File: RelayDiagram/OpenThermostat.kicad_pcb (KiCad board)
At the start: 2 copper layers, 81 parts, among them J1 Conn_01x08_Female, J2 Conn_01x15_Female, J3 Conn_01x15_Female, J4 Conn_01x09_Female, Q1 Q_NMOS_DGS, Q10 Q_NMOS_DGS, Q11 Q_NMOS_DGS, Q12 Q_NMOS_DGS, Q2 Q_NMOS_DGS, Q3 Q_NMOS_DGS, Q4 Q_NMOS_DGS, Q5 Q_NMOS_DGS, Q6 Q_NMOS_DGS, Q7 Q_NMOS_DGS, Q8 Q_NMOS_DGS, Q9 Q_NMOS_DGS, U1 PCF8574, U3 DHT11, U4 EE2-3TNU-L_DPDT_Relay, U5 EE2-3TNU-L_DPDT_Relay, U6 EE2-3TNU-L_DPDT_Relay, U7 EE2-3TNU-L_DPDT_Relay, U8 EE2-3TNU-L_DPDT_Relay, U9 EE2-3TNU-L_DPDT_Relay

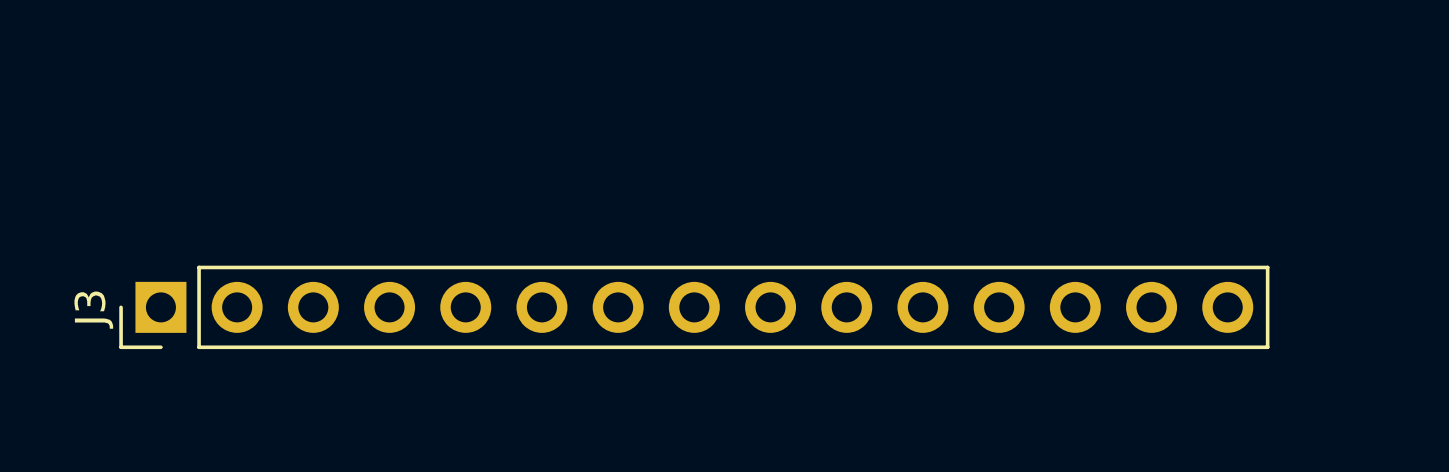
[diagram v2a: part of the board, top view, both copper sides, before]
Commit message: Minor routing changes and placeholder LCD footprint added
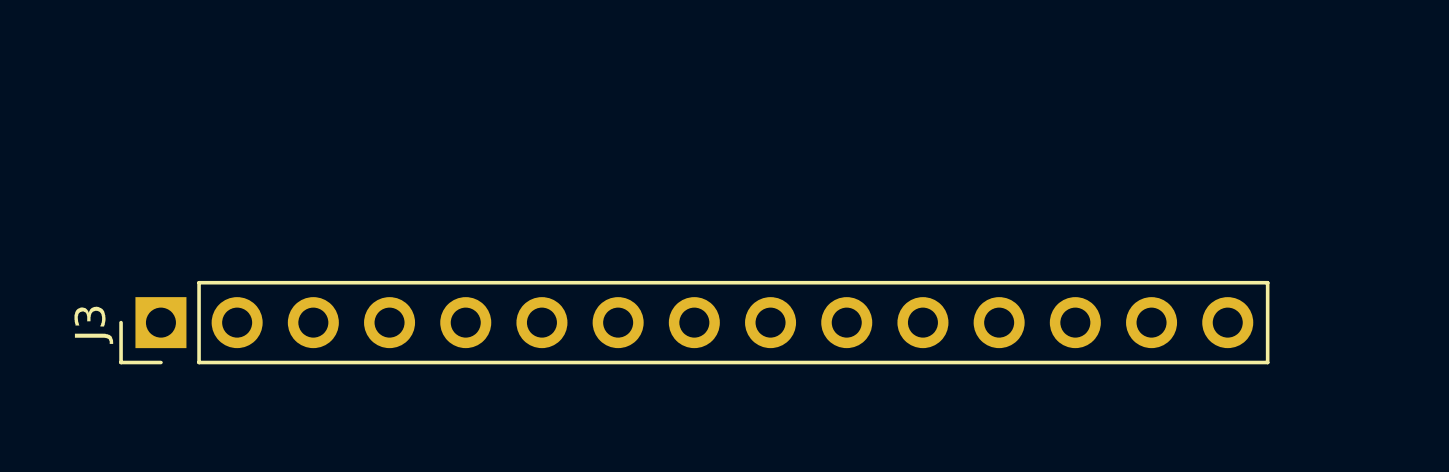
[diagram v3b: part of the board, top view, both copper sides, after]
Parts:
- moved J3 0.51 mm to (53.8, 126.2)
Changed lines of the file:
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@@
   )
   (setup
-    (last_trace_width 0.254)
+    (last_trace_width 0.25)
     (user_trace_width 0.254)
     (user_trace_width 0.508)
@@
   )
   (module Pin_Headers:Pin_Header_Straight_1x15_Pitch2.54mm (layer F.Cu)
-    (at 53.848 125.73 90)
+    (at 53.848 126.238 90)
     (descr "Through hole straight pin header, 1x15, 2.54mm pitch, single row")
     (tags "Through hole pin header THT 1x15 2.54mm single row")
@@
   )
   (dimension 27.94 (width 0.3) (layer F.SilkS)
-    (gr_text "27.940 mm" (at 51.376 113.538 90) (layer F.SilkS)
+    (gr_text "27.940 mm" (at 39.81 113.538 270) (layer F.SilkS)
       (effects (font (size 1.5 1.5) (thickness 0.3)))
     )
-    (feature1 (pts (xy 49.276 99.568) (xy 49.862421 99.568)))
-    (feature2 (pts (xy 49.276 127.508) (xy 49.862421 127.508)))
-    (crossbar (pts (xy 49.276 127.508) (xy 49.276 99.568)))
-    (arrow1a (pts (xy 49.276 99.568) (xy 49.862421 100.694504)))
-    (arrow1b (pts (xy 49.276 99.568) (xy 48.689579 100.694504)))
-    (arrow2a (pts (xy 49.276 127.508) (xy 49.862421 126.381496)))
-    (arrow2b (pts (xy 49.276 127.508) (xy 48.689579 126.381496)))
+    (feature1 (pts (xy 48.006 127.508) (xy 41.323579 127.508)))
+    (feature2 (pts (xy 48.006 99.568) (xy 41.323579 99.568)))
+    (crossbar (pts (xy 41.91 99.568) (xy 41.91 127.508)))
+    (arrow1a (pts (xy 41.91 127.508) (xy 41.323579 126.381496)))
+    (arrow1b (pts (xy 41.91 127.508) (xy 42.496421 126.381496)))
+    (arrow2a (pts (xy 41.91 99.568) (xy 41.323579 100.694504)))
+    (arrow2b (pts (xy 41.91 99.568) (xy 42.496421 100.694504)))
   )
   (via (at 63.1698 91.3892) (size 0.8) (drill 0.4) (layers F.Cu B.Cu) (net 25))

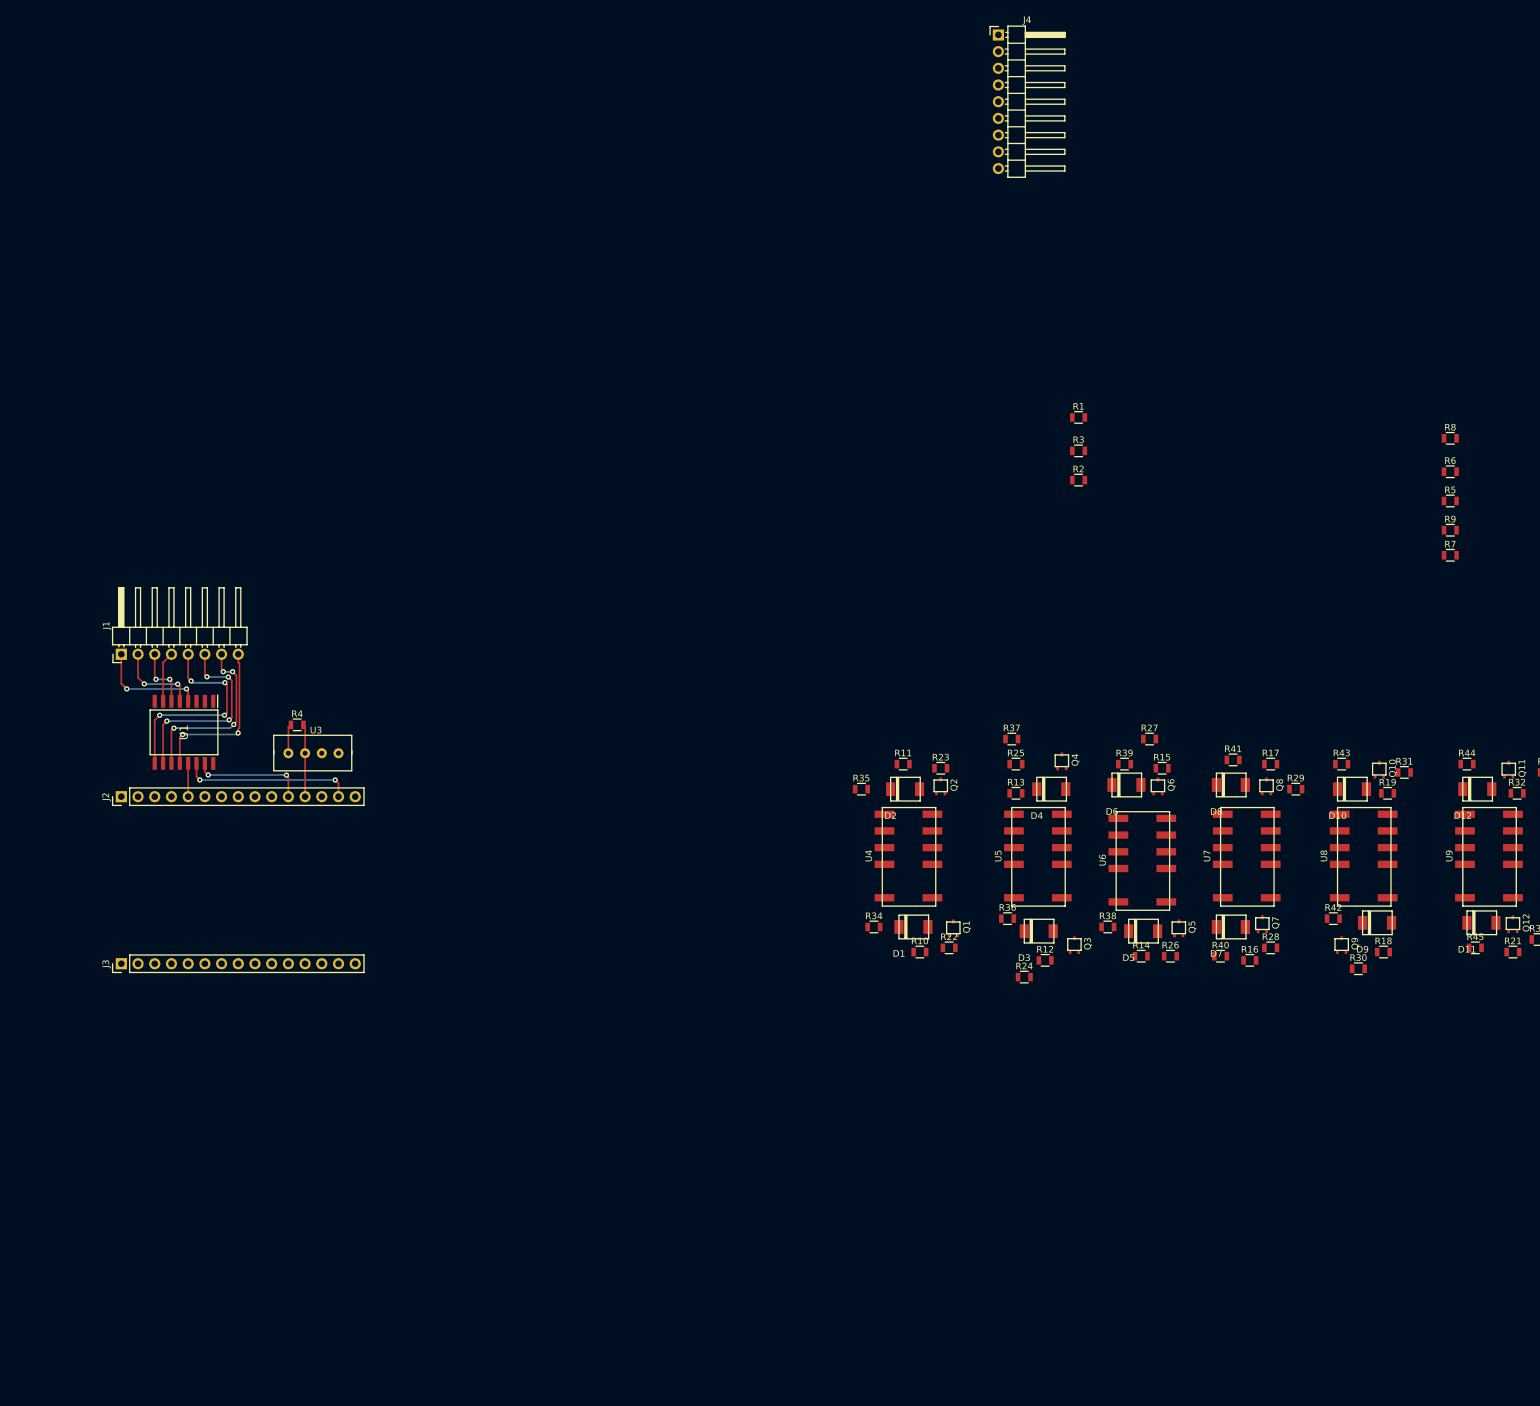
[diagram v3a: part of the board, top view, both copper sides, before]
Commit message: Added button footprints, PCB layout changes, changed schematic to fix relay coil polarity and also changed diode footprints.
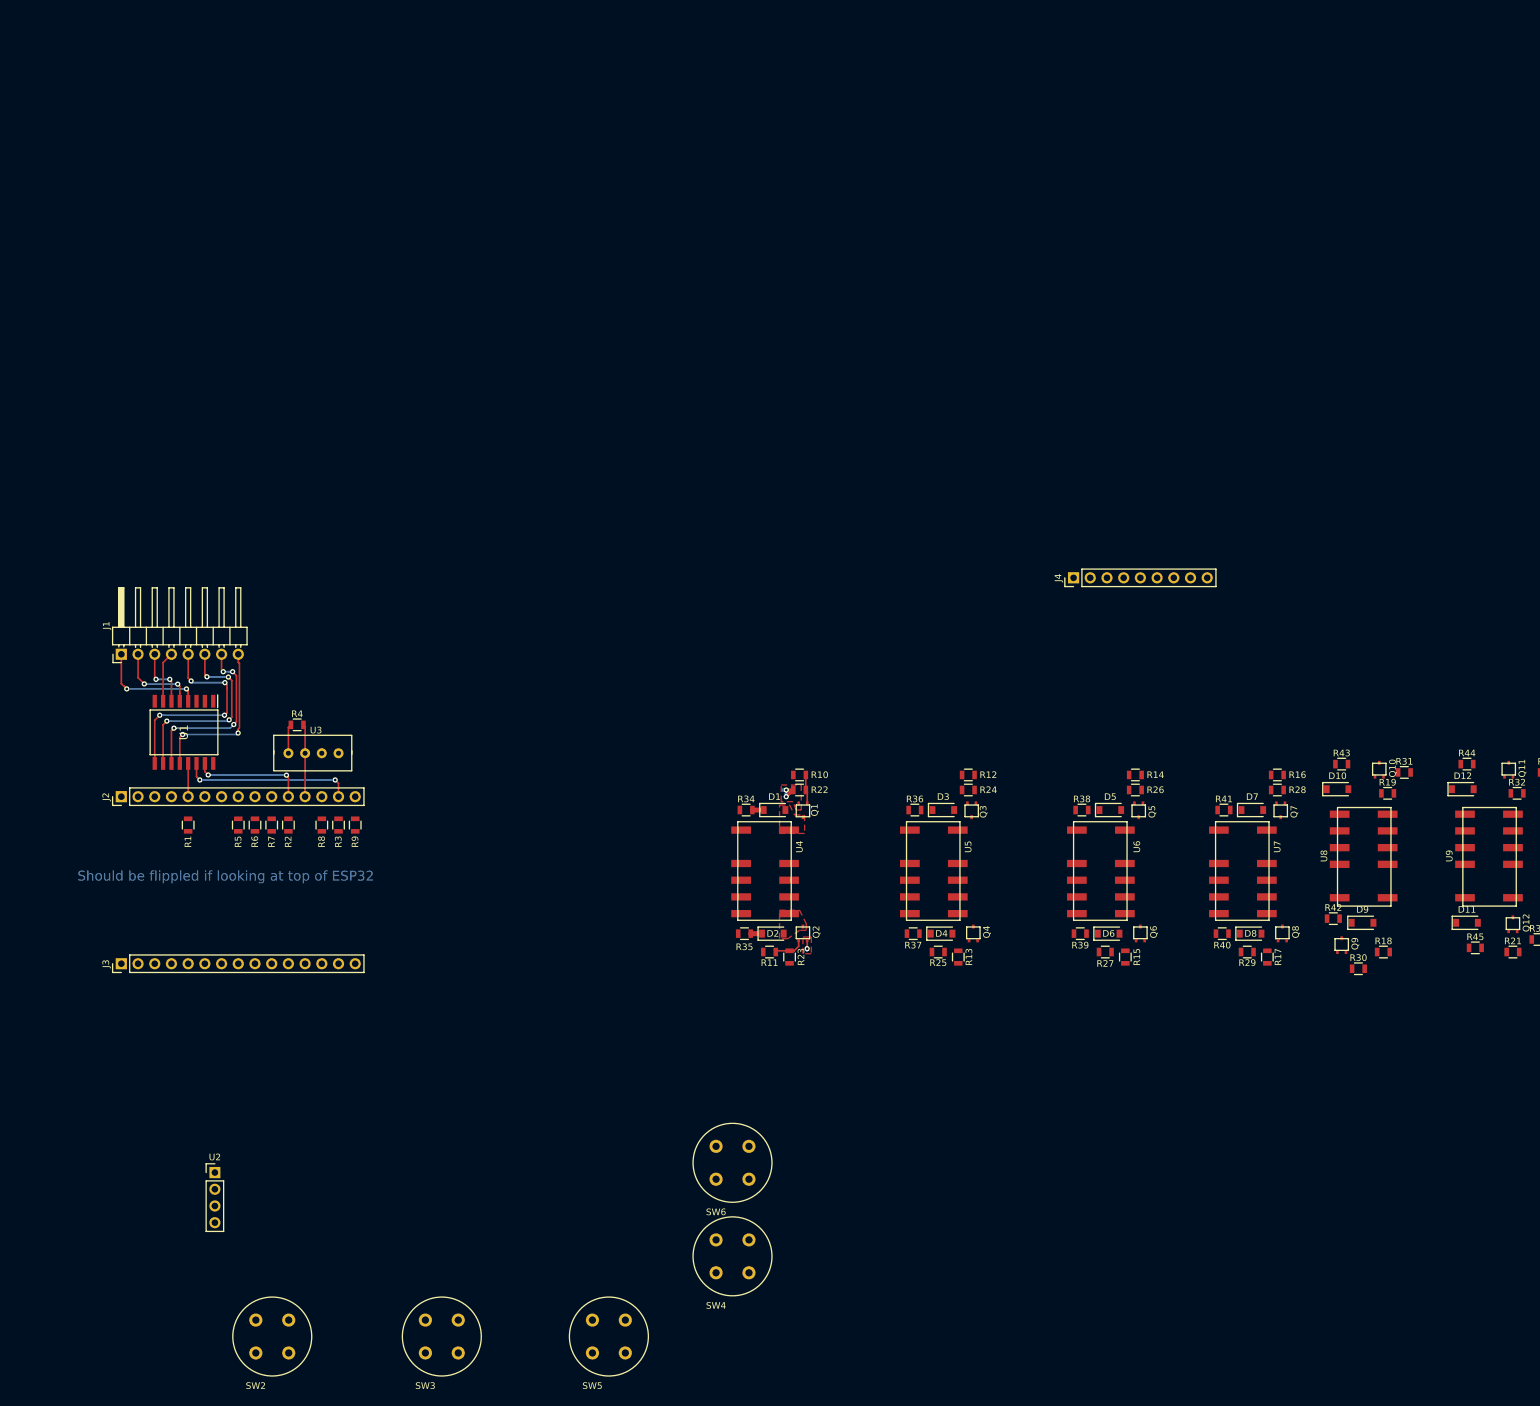
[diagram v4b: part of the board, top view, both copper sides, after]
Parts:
- added SW2: SW_Push, SeniorDesign:Pushbutton-KS-01Q-01, F.Cu at (74.3, 185.4)
- added SW3: SW_Push, SeniorDesign:Pushbutton-KS-01Q-01, F.Cu at (100.1, 185.4)
- added SW4: SW_Push, SeniorDesign:Pushbutton-KS-01Q-01, F.Cu at (144.3, 173.2)
- added SW5: SW_Push, SeniorDesign:Pushbutton-KS-01Q-01, F.Cu at (125.5, 185.4)
- added SW6: SW_Push, SeniorDesign:Pushbutton-KS-01Q-01, F.Cu at (144.3, 159.0)
- added U2: LCD, Pin_Headers:Pin_Header_Straight_1x04_Pitch2.54mm, F.Cu at (68.1, 158.0)
- D1, D10, D11, D12, D2, D3, D4, D5, D6, D7, D8, D9: footprint SeniorDesign:SOD-128-Diode -> Diodes_SMD:D_SOD-123
- J4: footprint Pin_Headers:Pin_Header_Angled_1x09_Pitch2.54mm -> Pin_Headers:Pin_Header_Straight_1x09_Pitch2.54mm
- moved R5 190.8 mm to (71.6, 105.2), turned to 270 degrees
- moved R6 189.5 mm to (74.2, 105.2), turned to 270 degrees
- moved R7 183.8 mm to (76.7, 105.2), turned to 270 degrees
- moved R8 181.4 mm to (84.3, 105.2), turned to 270 degrees
- moved R9 172.4 mm to (89.4, 105.2), turned to 270 degrees
- moved R1 148.9 mm to (64.0, 105.2), turned to 270 degrees
- moved R2 131.1 mm to (79.2, 105.2), turned to 270 degrees
- moved R3 126.1 mm to (86.9, 105.2), turned to 90 degrees
- moved J4 83.3 mm to (198.6, 67.6), turned to 90 degrees
- moved R23 36.8 mm to (155.4, 125.2), turned to 270 degrees
- moved R11 35.1 mm to (152.4, 124.5), turned to 180 degrees
- moved R37 33.2 mm to (174.2, 121.7)
- moved R27 33.1 mm to (203.5, 124.5), turned to 180 degrees
- moved R22 33.1 mm to (157.0, 99.8), turned to 180 degrees
- moved R10 32.5 mm to (157.0, 97.5), turned to 180 degrees
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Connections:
- U4 pad 1: Net-(D1-Pad2) -> +5V
- U4 pad 12: +5V -> Net-(D1-Pad2)
- U4 pad 6: Net-(D2-Pad2) -> +5V
- U4 pad 7: +5V -> Net-(D2-Pad2)
- U5 pad 1: Net-(D3-Pad2) -> +5V
- U5 pad 12: +5V -> Net-(D3-Pad2)
- U5 pad 6: Net-(D4-Pad2) -> +5V
- U5 pad 7: +5V -> Net-(D4-Pad2)
- U6 pad 1: Net-(D5-Pad2) -> +5V
- U6 pad 12: +5V -> Net-(D5-Pad2)
- U6 pad 6: Net-(D6-Pad2) -> +5V
- U6 pad 7: +5V -> Net-(D6-Pad2)
- U7 pad 1: Net-(D7-Pad2) -> +5V
- U7 pad 12: +5V -> Net-(D7-Pad2)
- U7 pad 6: Net-(D8-Pad2) -> +5V
- U7 pad 7: +5V -> Net-(D8-Pad2)
- U8 pad 1: Net-(D9-Pad2) -> +5V
- U8 pad 12: +5V -> Net-(D9-Pad2)
- U8 pad 6: Net-(D10-Pad2) -> +5V
- U8 pad 7: +5V -> Net-(D10-Pad2)
- U9 pad 1: Net-(D11-Pad2) -> +5V
- U9 pad 12: +5V -> Net-(D11-Pad2)
- U9 pad 6: Net-(D12-Pad2) -> +5V
- U9 pad 7: +5V -> Net-(D12-Pad2)
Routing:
- net GND: track 0.00 -> 5.26 mm, vias 0 -> 3
- net Net-(Q2-Pad2): track 0.00 -> 4.75 mm
- net Net-(Q1-Pad2): track 0.00 -> 4.40 mm
- net Net-(D2-Pad1): track 0.00 -> 1.72 mm
- net Net-(D1-Pad1): track 0.00 -> 1.72 mm
- added copper zone on F.Cu, net GND
- added copper zone on F.Cu, net Net-(D1-Pad2)
- added copper zone on F.Cu, net Net-(D2-Pad2)
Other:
- board text added: "Should be flippled if looking at top of ESP32"

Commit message: Created better LCD footprint(still needs double checking), flipped I/O Expander circuitry
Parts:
- added Ref**: Pin_Header_Angled_1x04_Pitch2.54mm, SeniorDesignLibrary:LCD, F.Cu at (138.9, 63.3)
- moved R35 125.9 mm to (269.0, 158.2), turned to 90 degrees
- moved R11 123.1 mm to (271.8, 154.4), turned to 270 degrees
- moved D2 120.5 mm to (269.0, 153.9), turned to 90 degrees
- moved R23 120.0 mm to (272.6, 151.3), turned to 0 degrees
- moved U4 117.7 mm to (253.3, 158.7), turned to 0 degrees
- moved Q2 115.7 mm to (270.1, 149.3), turned to 90 degrees
- moved R34 115.4 mm to (250.2, 157.9), turned to 90 degrees
- moved D1 109.5 mm to (250.2, 153.6), turned to 90 degrees
- moved U2 106.5 mm to (92.5, 54.4)
- moved Q1 103.3 mm to (249.2, 149.3), turned to 270 degrees
- moved R22 103.1 mm to (247.2, 149.8), turned to 270 degrees
- moved R10 102.3 mm to (244.9, 149.8), turned to 270 degrees
- moved R37 95.4 mm to (269.0, 132.5), turned to 90 degrees
- moved R25 93.9 mm to (271.8, 128.7), turned to 270 degrees
- moved R13 91.5 mm to (272.6, 125.7), turned to 0 degrees
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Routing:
- net Net-(J2-Pad11): track 17.3 -> 24.0 mm
- net Net-(J2-Pad14): track 26.0 -> 30.6 mm
- net Net-(J2-Pad5): track 5.05 -> 6.25 mm
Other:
- board text removed: "Should be flippled if looking at top of ESP32"
